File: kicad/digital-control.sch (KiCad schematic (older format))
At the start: 33 parts, among them J1 SWD, J4 USB_OTG, U1 STM32F042KxT, U2 USBLC6-2

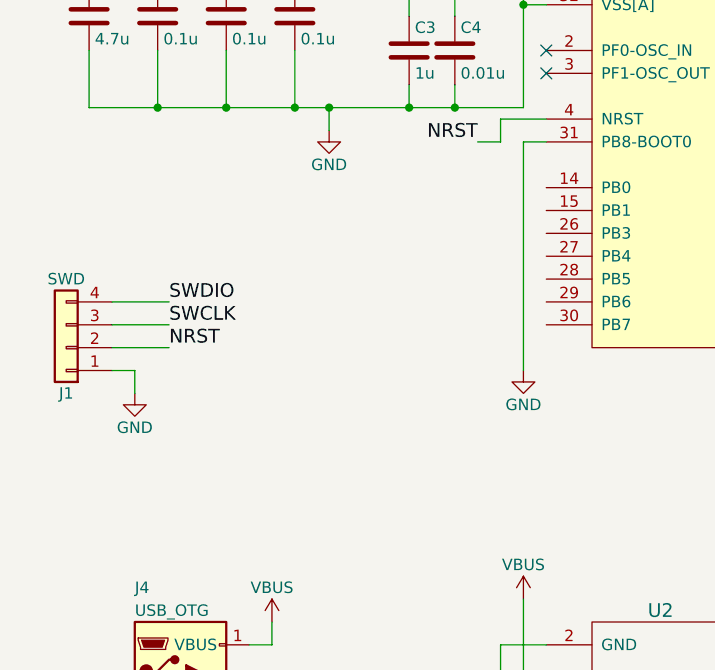
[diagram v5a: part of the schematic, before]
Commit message: Created shift register circuitry and imported footprints
I think 5MHz to 10MHz is the theoretical maximum of this circuit. Actual
frequency will probably be around 5MHz or somewhat less given the signal
integrity issues on a 2-layer board with this many plane breaks.

Created footprints for button and HTSSOP

The HTSSOP footprint is special because I plan to hand solder, so I
added excessive thermal vias and a bare pad on the backside.

The netlist is imported to the PCB, but only the switches are placed.
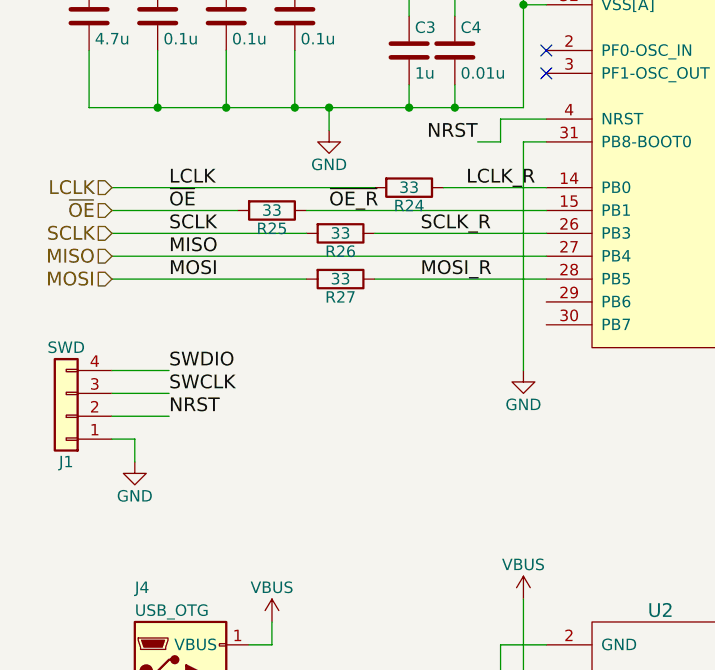
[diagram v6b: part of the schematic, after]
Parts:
- added R24, R25, R26, R27: 33, Resistors_SMD:R_0402, symbol R
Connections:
- net LCLK_R: now reaches U1.14 (PB0)
- net LCLK_R: now also R24.1
- net ~OE_R: now reaches U1.15 (PB1)
- net ~OE_R: now also R25.1
- net SCLK_R: now reaches U1.26 (PB3)
- net SCLK_R: now also R26.1
- net MISO: now reaches U1.27 (PB4)
- net MOSI_R: now reaches U1.28 (PB5)
- net MOSI_R: now also R27.1
- new net LCLK: R24.2
- new net MOSI: R27.2
- new net SCLK: R26.2
- new net ~OE: R25.2
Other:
- moved on the sheet: J1
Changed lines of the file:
@@
 L Conn_01x04 J1
 U 1 1 5B3C620F
-P 800 3400
-F 0 "J1" H 800 3600 50  0000 C CNN
-F 1 "SWD" H 800 3100 50  0000 C CNN
-F 2 "midi-fader:JST-SH-4" H 800 3400 50  0001 C CNN
-F 3 "" H 800 3400 50  0001 C CNN
-F 4 "455-1790-1-ND" H 800 3400 60  0001 C CNN "Part No."
-	1    800  3400
+P 800 3700
+F 0 "J1" H 800 3900 50  0000 C CNN
+F 1 "SWD" H 800 3400 50  0000 C CNN
+F 2 "midi-fader:JST-SH-4" H 800 3700 50  0001 C CNN
+F 3 "" H 800 3700 50  0001 C CNN
+F 4 "455-1790-1-ND" H 800 3700 60  0001 C CNN "Part No."
+	1    800  3700
 	-1   0    0    1
 $EndComp
@@
 L GND #PWR08
 U 1 1 5B3CF2D7
-P 1100 3600
-F 0 "#PWR08" H 1100 3350 50  0001 C CNN
-F 1 "GND" H 1100 3450 50  0000 C CNN
-F 2 "" H 1100 3600 50  0001 C CNN
-F 3 "" H 1100 3600 50  0001 C CNN
-	1    1100 3600
-	1    0    0    -1
-$EndComp
-Text Label 1250 3200 0    60   ~ 0
+P 1100 3900
+F 0 "#PWR08" H 1100 3650 50  0001 C CNN
+F 1 "GND" H 1100 3750 50  0000 C CNN
+F 2 "" H 1100 3900 50  0001 C CNN
+F 3 "" H 1100 3900 50  0001 C CNN
+	1    1100 3900
+	1    0    0    -1
+$EndComp
+Text Label 1250 3500 0    60   ~ 0
 SWDIO
-Text Label 1250 3300 0    60   ~ 0
+Text Label 1250 3600 0    60   ~ 0
 SWCLK
-Text Label 1250 3400 0    60   ~ 0
+Text Label 1250 3700 0    60   ~ 0
 NRST
 $Comp
@@
 Connection ~ 1800 2350
 Wire Wire Line
-	1000 3200 1250 3200
-Wire Wire Line
-	1000 3300 1250 3300
-Wire Wire Line
-	1000 3400 1250 3400
-Wire Wire Line
-	1000 3500 1100 3500
-Wire Wire Line
-	1100 3500 1100 3600
+	1000 3500 1250 3500
+Wire Wire Line
+	1000 3600 1250 3600
+Wire Wire Line
+	1000 3700 1250 3700
+Wire Wire Line
+	1000 3800 1100 3800
+Wire Wire Line
+	1100 3800 1100 3900
 Wire Wire Line
 	2800 3500 2800 2500
@@
 Wire Wire Line
 	10600 1000 9900 1000
+$Comp
+L R R26
+U 1 1 5B418F7B
+P 2000 2900
+F 0 "R26" V 2080 2900 50  0000 C CNN
+F 1 "33" V 2000 2900 50  0000 C CNN
+F 2 "Resistors_SMD:R_0402" V 1930 2900 50  0001 C CNN
+F 3 "" H 2000 2900 50  0001 C CNN
+	1    2000 2900
+	0    1    1    0
+$EndComp
+$Comp
+L R R27
+U 1 1 5B418FE2
+P 2000 3100
+F 0 "R27" V 2080 3100 50  0000 C CNN
+F 1 "33" V 2000 3100 50  0000 C CNN
+F 2 "Resistors_SMD:R_0402" V 1930 3100 50  0001 C CNN
+F 3 "" H 2000 3100 50  0001 C CNN
+	1    2000 3100
+	0    1    1    0
+$EndComp
+Wire Wire Line
+	2150 2900 2900 2900
+Text Label 2350 2900 0    60   ~ 0
+SCLK_R
+Text Label 2350 3100 0    60   ~ 0
+MOSI_R
+Wire Wire Line
+	2150 3100 2900 3100
+Text HLabel 1000 2900 0    60   Input ~ 0
+SCLK
+Wire Wire Line
+	1000 2900 1850 2900
+Text Label 1250 2900 0    60   ~ 0
+SCLK
+Text Label 1250 3100 0    60   ~ 0
+MOSI
+Wire Wire Line
+	1850 3100 1000 3100
+Text HLabel 1000 3100 0    60   Input ~ 0
+MOSI
+Text HLabel 1000 3000 0    60   Input ~ 0
+MISO
+Wire Wire Line
+	2900 3000 1000 3000
+Text Label 1250 3000 0    60   ~ 0
+MISO
+Text HLabel 1000 2700 0    60   Input ~ 0
+LCLK
+Text HLabel 1000 2800 0    60   Input ~ 0
+~OE
+$Comp
+L R R24
+U 1 1 5B41A105
+P 2300 2700
+F 0 "R24" V 2380 2700 50  0000 C CNN
+F 1 "33" V 2300 2700 50  0000 C CNN
+F 2 "Resistors_SMD:R_0402" V 2230 2700 50  0001 C CNN
+F 3 "" H 2300 2700 50  0001 C CNN
+	1    2300 2700
+	0    1    1    0
+$EndComp
+$Comp
+L R R25
+U 1 1 5B41A1B0
+P 1700 2800
+F 0 "R25" V 1780 2800 50  0000 C CNN
+F 1 "33" V 1700 2800 50  0000 C CNN
+F 2 "Resistors_SMD:R_0402" V 1630 2800 50  0001 C CNN
+F 3 "" H 1700 2800 50  0001 C CNN
+	1    1700 2800
+	0    1    1    0
+$EndComp
+Wire Wire Line
+	2450 2700 2900 2700
+Wire Wire Line
+	2150 2700 1000 2700
+Wire Wire Line
+	1000 2800 1550 2800
+Wire Wire Line
+	1850 2800 2900 2800
+Text Label 2550 2700 0    60   ~ 0
+LCLK_R
+Text Label 1950 2800 0    60   ~ 0
+~OE_R
+Text Label 1250 2700 0    60   ~ 0
+LCLK
+Text Label 1250 2800 0    60   ~ 0
+~OE
 $EndSCHEMATC

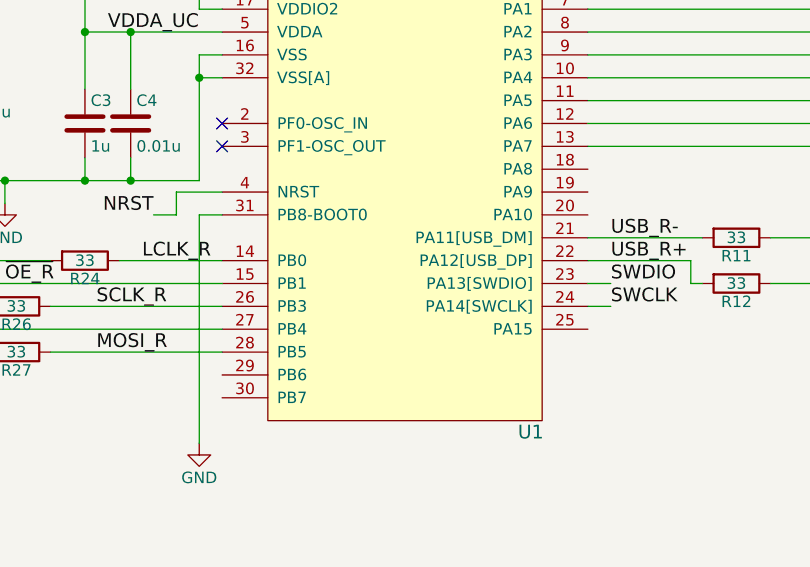
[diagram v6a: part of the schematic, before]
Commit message: Marked no-connects and changed some plane shapes
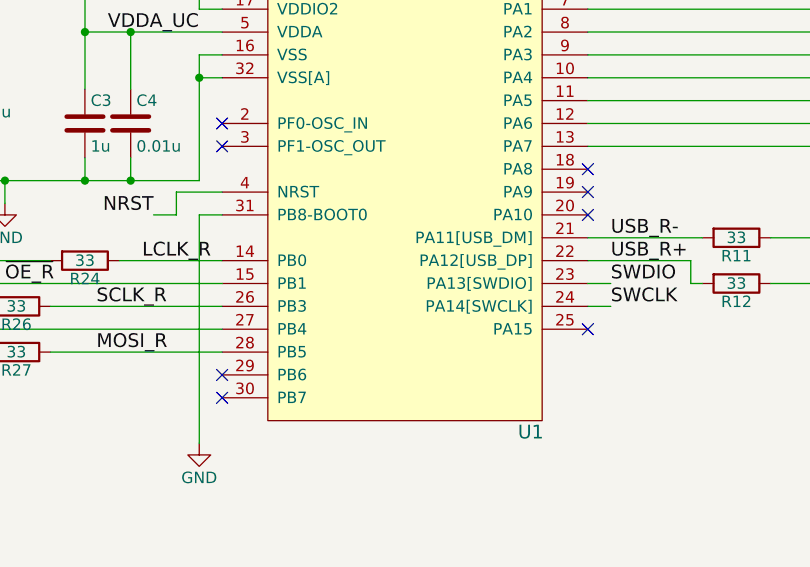
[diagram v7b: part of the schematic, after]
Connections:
- no-connect marks 3 -> 9
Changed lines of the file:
@@
 Text Label 1250 2800 0    60   ~ 0
 ~OE
+NoConn ~ 2900 3200
+NoConn ~ 2900 3300
+NoConn ~ 4500 2300
+NoConn ~ 4500 2400
+NoConn ~ 4500 2500
+NoConn ~ 4500 3000
 $EndSCHEMATC

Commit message: Added stub-removal resistors on clock lines, started cleaning silkscreen
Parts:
- C3: Part No. 1276-6524-1-ND -> 1276-1182-1-ND
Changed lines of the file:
@@
 F 2 "Capacitors_SMD:C_0603" H 2338 1950 50  0001 C CNN
 F 3 "" H 2300 2100 50  0001 C CNN
-F 4 "1276-6524-1-ND" H 2300 2100 60  0001 C CNN "Part No."
+F 4 "1276-1182-1-ND" H 2300 2100 60  0001 C CNN "Part No."
 	1    2300 2100
 	1    0    0    -1
